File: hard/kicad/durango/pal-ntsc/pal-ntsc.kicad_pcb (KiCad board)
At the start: 2 copper layers, 34 parts, among them J101 SCART, J103 ~CSYNC, J4 S-Video, J5 COMPOSITE, Q1 BC548, Q2 BC548, Q3 BC548, U1 AD724, Y1 3.58 MHz (PAL=4.43)

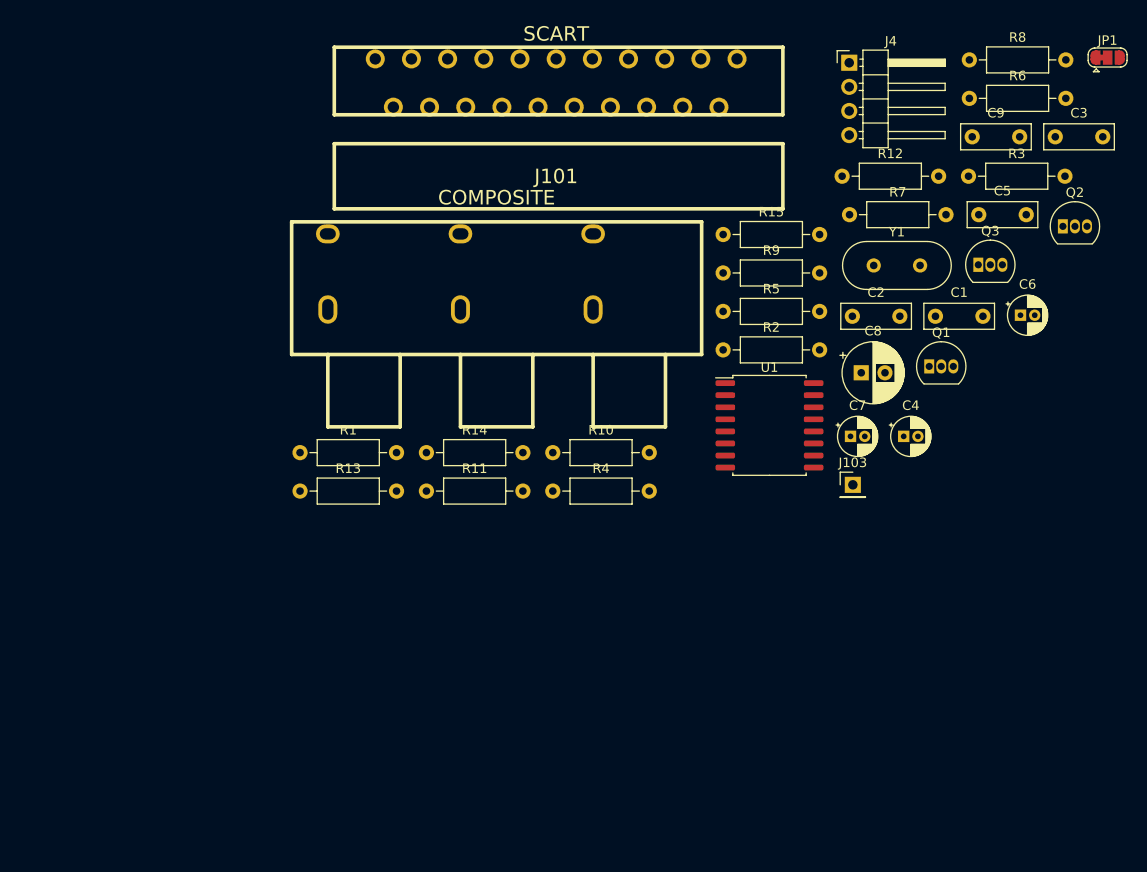
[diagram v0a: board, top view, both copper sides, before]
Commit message: preliminary PAL/NTSC encoder layout
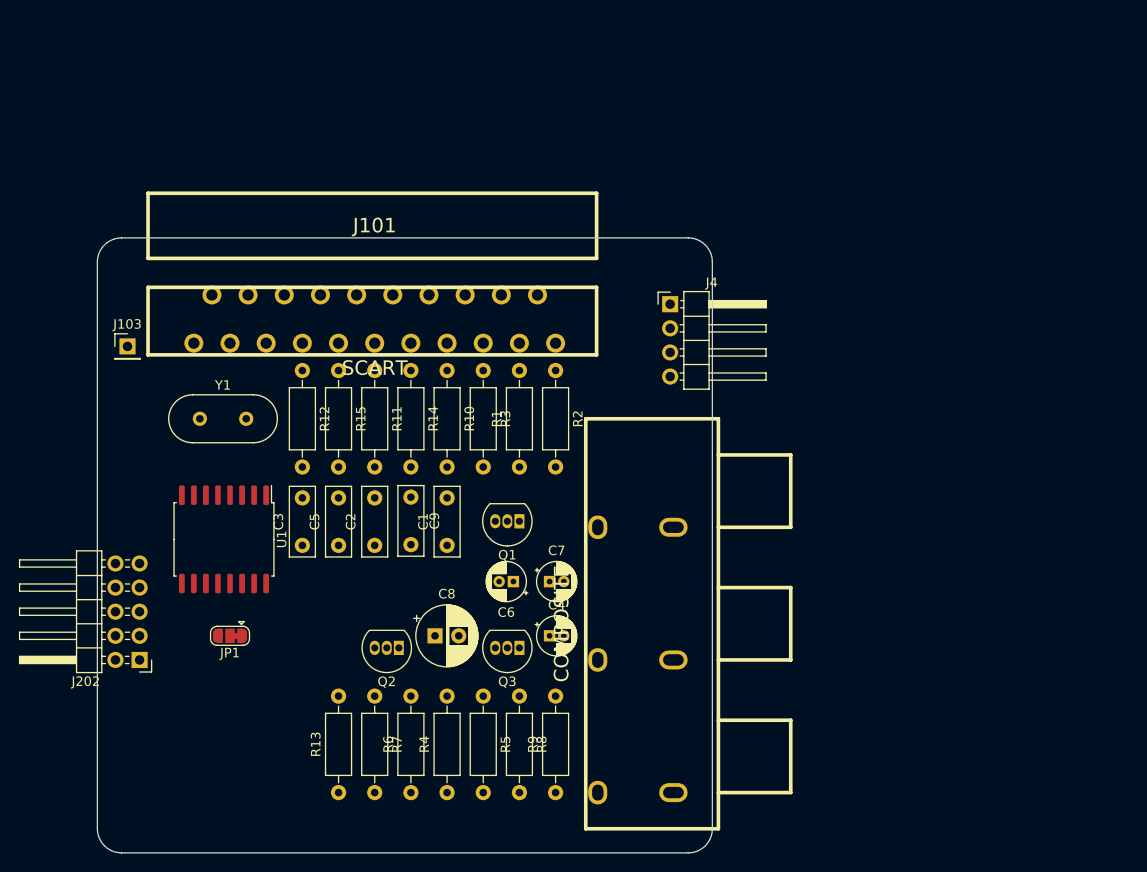
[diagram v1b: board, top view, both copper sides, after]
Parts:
- added J202: RGB, Connector_PinHeader_2.54mm:PinHeader_2x05_P2.54mm_Horizontal, F.Cu at (67.9, 94.0)
- moved JP1 110.7 mm to (77.5, 91.4), turned to 180 degrees
- moved R6 93.8 mm to (96.5, 108.0), turned to 90 degrees
- moved C3 90.2 mm to (85.1, 81.9), turned to 90 degrees
- moved Q2 82.8 mm to (95.2, 92.7), turned to 180 degrees
- moved R8 82.1 mm to (108.0, 97.8), turned to 270 degrees
- moved J103 77.8 mm to (66.7, 61.0)
- moved C5 75.9 mm to (88.9, 81.9), turned to 90 degrees
- moved Y1 72.8 mm to (74.3, 68.6)
- moved R7 71.2 mm to (92.7, 97.8), turned to 270 degrees
- moved C9 70.2 mm to (96.5, 76.8), turned to 270 degrees
- moved Q3 63.0 mm to (108.0, 92.7), turned to 180 degrees
- moved R12 60.4 mm to (85.1, 63.5), turned to 270 degrees
- moved C6 60.3 mm to (107.3, 85.7), turned to 180 degrees
- moved U1 58.7 mm to (76.8, 81.3), turned to 270 degrees
- moved R9 57.5 mm to (111.8, 108.0), turned to 90 degrees
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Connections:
- net Net-(J103-Pad1) renamed /~CSYNC
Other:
- board outline added: 64.8 x 64.8 mm
